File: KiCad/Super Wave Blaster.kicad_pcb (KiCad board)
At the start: 2 copper layers, 40 x 21.2 mm, 21 parts, among them J1 EIAJ_Input, J2 PCM5102_I2S, J3 PCM5102_Audio, J4 Power Input, J5 Audio_Jack, J6 Power Input, J7 Audio Out, U1 TLV73333PDBV, U2 CD74HCT14PWR, U3 SN74HC595PWR, U4 SN74LVC8T245PWR

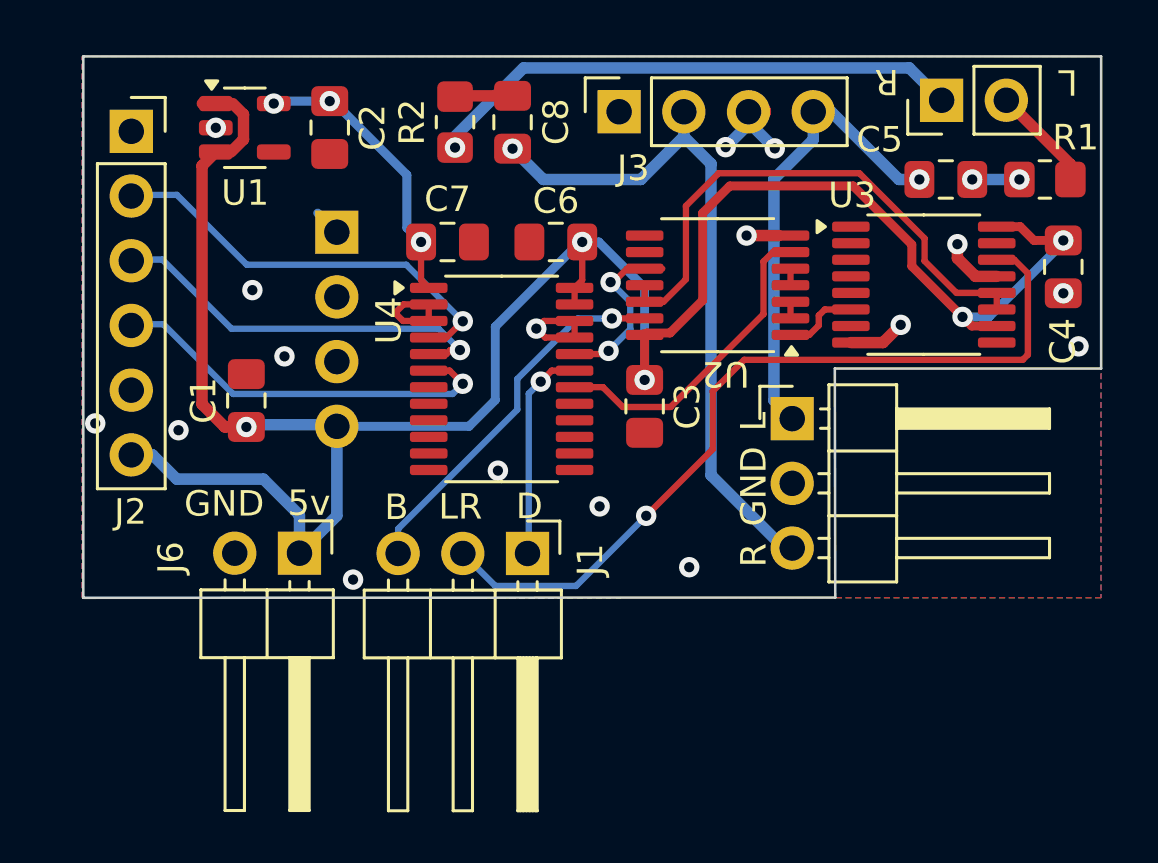
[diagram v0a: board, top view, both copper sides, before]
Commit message: V1.5
Refactored for underside mounting only and optional expansion for S/PDIF output. Full PCM5102A integration. Optimized audio quality.
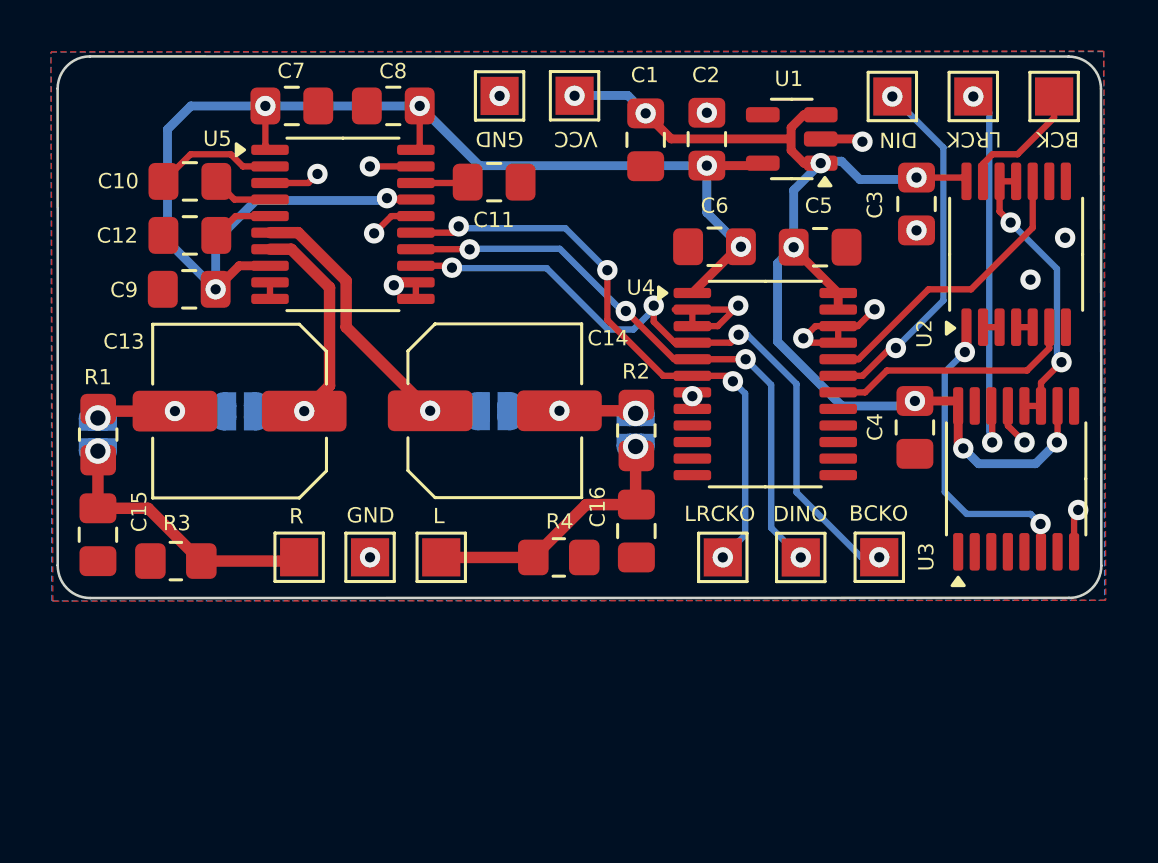
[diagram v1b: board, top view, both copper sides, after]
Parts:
- removed J1: EIAJ_Input, Connector_PinHeader_2.54mm:PinHeader_1x03_P2.54mm_Horizontal
- removed J2: PCM5102_I2S, Connector_PinSocket_2.54mm:PinSocket_1x06_P2.54mm_Vertical
- removed J3: PCM5102_Audio, Connector_PinSocket_2.54mm:PinSocket_1x04_P2.54mm_Vertical
- removed J4: Power Input, Connector_PinHeader_2.54mm:PinHeader_1x04_P2.54mm_Vertical
- removed J5: Audio_Jack, Connector_PinHeader_2.54mm:PinHeader_1x03_P2.54mm_Horizontal
- removed J6: Power Input, Connector_PinHeader_2.54mm:PinHeader_1x02_P2.54mm_Horizontal
- removed J7: Audio Out, Connector_PinHeader_2.54mm:PinHeader_1x02_P2.54mm_Vertical
- added C10: 2.2uf, Capacitor_SMD:C_0805_2012Metric_Pad1.18x1.45mm_HandSolder, F.Cu at (118.5, 68.7)
- added C11: 0.1uf, Capacitor_SMD:C_0805_2012Metric_Pad1.18x1.45mm_HandSolder, F.Cu at (130.4, 68.7)
- added C12: 2.2uf, Capacitor_SMD:C_0805_2012Metric_Pad1.18x1.45mm_HandSolder, F.Cu at (118.5, 70.8)
- added C13: 1uf, Capacitor_SMD:C_Elec_6.3x5.8, F.Cu at (120.4, 77.7)
- added C14: 1uf, Capacitor_SMD:C_Elec_6.3x5.8, F.Cu at (130.5, 77.7)
- added C15: 43pf, Capacitor_SMD:C_0805_2012Metric_Pad1.18x1.45mm_HandSolder, F.Cu at (114.9, 82.5)
- added C16: 43pf, Capacitor_SMD:C_0805_2012Metric_Pad1.18x1.45mm_HandSolder, F.Cu at (136.0, 82.4)
- added C9: 0.1uf, Capacitor_SMD:C_0805_2012Metric_Pad1.18x1.45mm_HandSolder, F.Cu at (118.5, 72.9)
- added JP1: ~, Jumper:SolderJumper-2_P1.3mm_Open_RoundedPad1.0x1.5mm, B.Cu at (114.9, 78.6)
- added JP2: ~, Jumper:SolderJumper-2_P1.3mm_Open_RoundedPad1.0x1.5mm, B.Cu at (136.0, 78.4)
- added JP3: ~, Jumper:SolderJumper-2_P1.3mm_Open_RoundedPad1.0x1.5mm, B.Cu at (120.5, 77.7)
- added JP4: ~, Jumper:SolderJumper-2_P1.3mm_Open_RoundedPad1.0x1.5mm, B.Cu at (130.4, 77.7)
- added R3: 100k, Resistor_SMD:R_0805_2012Metric_Pad1.20x1.40mm_HandSolder, F.Cu at (117.9, 83.6)
- added R4: 100k, Resistor_SMD:R_0805_2012Metric_Pad1.20x1.40mm_HandSolder, F.Cu at (133.0, 83.4)
- added TP1: VCC, TestPoint:TestPoint_Pad_1.5x1.5mm, F.Cu at (133.6, 65.3)
- added TP10: BCLKO, TestPoint:TestPoint_Pad_1.5x1.5mm, F.Cu at (145.5, 83.4)
- added TP11: GND, TestPoint:TestPoint_Pad_1.5x1.5mm, F.Cu at (125.6, 83.4)
- added TP2: GND, TestPoint:TestPoint_Pad_1.5x1.5mm, F.Cu at (130.6, 65.3)
- added TP3: A-Left, TestPoint:TestPoint_Pad_1.5x1.5mm, F.Cu at (128.3, 83.4)
- added TP4: A-Left, TestPoint:TestPoint_Pad_1.5x1.5mm, F.Cu at (122.8, 83.4)
- added TP5: DIN, TestPoint:TestPoint_Pad_1.5x1.5mm, F.Cu at (146.1, 65.3)
- added TP6: LRCLK, TestPoint:TestPoint_Pad_1.5x1.5mm, F.Cu at (149.2, 65.3)
- added TP7: BCLK, TestPoint:TestPoint_Pad_1.5x1.5mm, F.Cu at (152.4, 65.3)
- added TP8: DINO, TestPoint:TestPoint_Pad_1.5x1.5mm, F.Cu at (142.5, 83.4)
- added TP9: LRCLKO, TestPoint:TestPoint_Pad_1.5x1.5mm, F.Cu at (139.4, 83.4)
- added U5: PCM5102A, Package_SO:TSSOP-20_4.4x6.5mm_P0.65mm, F.Cu at (124.5, 70.3)
- C5, C8: value 1uf -> 0.1uf
- moved R1 38.5 mm to (114.9, 78.6), turned to 90 degrees
- moved U1 21.5 mm to (142.1, 67.0), turned to 180 degrees
- moved C1 18.7 mm to (136.4, 67.0), turned to -90 degrees
- moved C2 14.8 mm to (138.8, 67.0), turned to 90 degrees
- moved R2 14.0 mm to (136.0, 78.4), turned to 90 degrees
- moved C3 13.3 mm to (147.0, 69.5)
- moved U2 11.8 mm to (150.9, 71.5), turned to 90 degrees
- moved U4 10.4 mm to (141.1, 76.6)
- moved C4 8.58 mm to (146.9, 78.3)
- moved U3 8.44 mm to (150.9, 80.3), turned to 90 degrees
- moved C7 8.12 mm to (122.5, 65.7)
- moved C6 6.23 mm to (139.1, 71.2)
- moved C5 5.61 mm to (143.2, 71.2)
- moved C8 4.73 mm to (126.5, 65.7), turned to 180 degrees
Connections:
- C5 pad 1: AUDIO_L -> VCC
- C5 pad 2: Net-(C5-Pad2) -> GND
- C6 pad 1: VCC -> VDD
- C8 pad 1: AUDIO_R -> VDD
- C8 pad 2: Net-(C8-Pad2) -> GND
- R1 pad 1: Net-(C5-Pad2) -> AUDIO_R
- R2 pad 1: Net-(C8-Pad2) -> AUDIO_L
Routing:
- net VDD: track 11.3 -> 54.7 mm, vias 3 -> 6
- net VCC: track 87.9 -> 45.4 mm, vias 5 -> 8
- net LRCK_EIAJ: track 32.4 -> 14.9 mm, vias 1 -> 2
- net Net-(JP2-A): track 21.2 -> 4.97 mm, vias 1 -> 2
- net AUDIO_R: track 27.0 -> 11.2 mm
- net Net-(JP4-A): track 0.00 -> 12.0 mm, vias 0 -> 1
- net BCK_VDD: track 16.0 -> 27.1 mm, vias 1 -> 4
- net Net-(JP3-A): track 0.00 -> 10.7 mm, vias 0 -> 1
- net BCK_INV: track 21.4 -> 11.5 mm, vias 0 -> 2
- net BCK_EIAJ: track 14.8 -> 5.06 mm, vias 1 -> 0
- net LRCK_VDD: track 15.2 -> 24.5 mm, vias 1 -> 4
- net Net-(U2-1A): track 3.01 -> 12.2 mm, vias 0 -> 2
- net DIN_VDD: track 15.0 -> 23.4 mm, vias 1 -> 4
- net AUDIO_L: track 18.2 -> 10.8 mm
- net DIN_EIAJ: track 8.47 -> 14.2 mm, vias 1 -> 2
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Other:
- board size 40 x 21.2 mm -> 41 x 21.3 mm
- board text added: "(JP1 JP2 = X R3 R4) (JP3 JP4 = X C13 C14)"
- board text added: "BCKO"
- board text added: "DINO"
- board text added: "LRCKO"
- board text added: "Super Wave Blaster V1.5 github.com/RetroLoom/Super-Wave-Blaster"
- board text added: "VCC"
- board text removed: "+"
- board text removed: "-"
- board text removed: "5v"
- board text removed: "B"
- board text removed: "D"
- board text removed: "LR"
- board text removed: "Super Wave Blaster"
- board text removed: "V1.4"

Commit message: V1.6
Refactor analog circuit with 0.1uf coupling and 100k pull down.
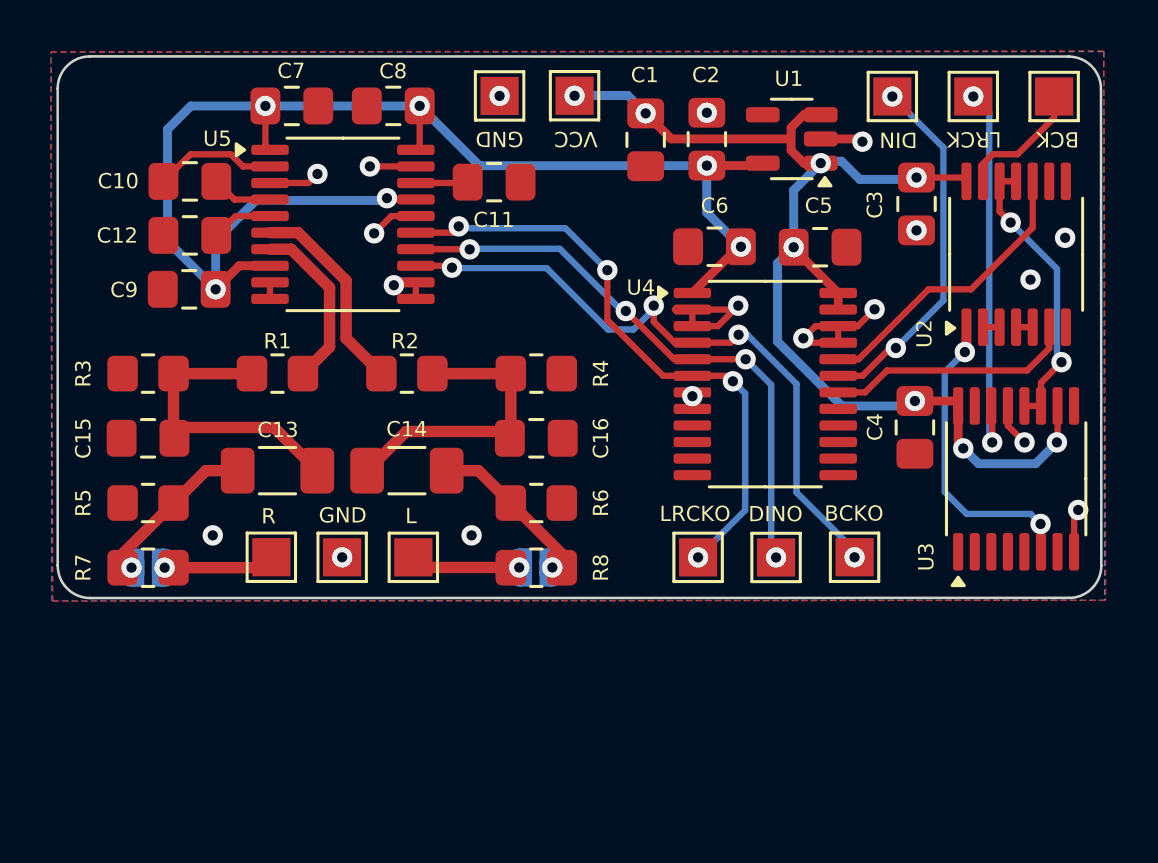
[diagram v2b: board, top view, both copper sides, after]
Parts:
- removed JP3, JP4: ~, Jumper:SolderJumper-2_P1.3mm_Open_RoundedPad1.0x1.5mm
- added R5: 100k, Resistor_SMD:R_0805_2012Metric_Pad1.20x1.40mm_HandSolder, F.Cu at (116.8, 81.3)
- added R6: 100k, Resistor_SMD:R_0805_2012Metric_Pad1.20x1.40mm_HandSolder, F.Cu at (132.1, 81.3)
- added R7: 24k, Resistor_SMD:R_0805_2012Metric_Pad1.20x1.40mm_HandSolder, F.Cu at (116.8, 83.8)
- added R8: 24k, Resistor_SMD:R_0805_2012Metric_Pad1.20x1.40mm_HandSolder, F.Cu at (132.1, 83.8)
- C13, C14: value 1uf -> 0.1uf; footprint Capacitor_SMD:C_Elec_6.3x5.8 -> Capacitor_SMD:C_1206_3216Metric_Pad1.33x1.80mm_HandSolder
- C15, C16: value 43pf -> 2.2nf
- R1, R2: value 24k -> 470
- R3, R4: value 100k -> 470
- moved R2 9.28 mm to (127.0, 76.2), turned to 180 degrees
- moved R3 7.44 mm to (116.8, 76.2)
- moved R1 7.43 mm to (121.9, 76.2), turned to 0 degrees
- moved R4 7.27 mm to (132.1, 76.2)
- moved JP2 6.67 mm to (132.1, 83.8), turned to 180 degrees
- moved JP1 5.59 mm to (116.8, 83.8), turned to 0 degrees
- moved C16 5.35 mm to (132.1, 78.7), turned to 0 degrees
- moved C15 4.27 mm to (116.8, 78.7), turned to 0 degrees
- moved C14 4.18 mm to (127.0, 80.0), turned to 180 degrees
- moved C13 2.77 mm to (121.9, 80.0), turned to 0 degrees
- moved TP11 1.09 mm to (124.5, 83.4)
- moved TP4 1.09 mm to (121.7, 83.4)
- moved TP3 1.09 mm to (127.3, 83.4)
- moved TP10 0.97 mm to (144.6, 83.4)
- moved TP8 0.97 mm to (141.5, 83.4)
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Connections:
- C13 pad 1: Net-(JP3-A) -> Net-(JP1-A)
- C13 pad 2: Net-(JP1-A) -> Net-(C13-Pad2)
- C14 pad 1: Net-(JP4-A) -> Net-(JP2-A)
- C14 pad 2: Net-(JP2-A) -> Net-(C14-Pad2)
- C15 pad 2: AUDIO_R -> Net-(C13-Pad2)
- C16 pad 1: AUDIO_L -> Net-(C14-Pad2)
- R1 pad 1: AUDIO_R -> Net-(C13-Pad2)
- R1 pad 2: Net-(JP1-A) -> Net-(U5-OUTR)
- R2 pad 1: AUDIO_L -> Net-(C14-Pad2)
- R2 pad 2: Net-(JP2-A) -> Net-(U5-OUTL)
- R3 pad 1: AUDIO_R -> Net-(C13-Pad2)
- R4 pad 2: AUDIO_L -> Net-(C14-Pad2)
- U5 pad 6: Net-(JP4-A) -> Net-(U5-OUTL)
- U5 pad 7: Net-(JP3-A) -> Net-(U5-OUTR)
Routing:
- net Net-(C13-Pad2): track 0.00 -> 12.1 mm
- net Net-(JP4-A): track 12.0 -> 0.00 mm, vias 1 -> 0
- net Net-(C14-Pad2): track 0.00 -> 12.0 mm
- net Net-(JP3-A): track 10.7 -> 0.00 mm, vias 1 -> 0
- net Net-(U5-OUTL): track 0.00 -> 7.99 mm
- net AUDIO_R: track 11.2 -> 4.36 mm
- net Net-(U5-OUTR): track 0.00 -> 6.77 mm
- net AUDIO_L: track 10.8 -> 4.32 mm
- net Net-(JP2-A): track 4.97 -> 6.41 mm, vias 2 -> 1
- net Net-(JP1-A): track 5.00 -> 6.41 mm, vias 2 -> 1
- net BCK_VDD: track 27.1 -> 26.3 mm
- net GND: vias 17 -> 19
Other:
- board text added: "(JP1 JP2 = X R7 R8)"
- board text added: "Super Wave Blaster V1.6 github.com/RetroLoom/Super-Wave-Blaster"
- board text removed: "(JP1 JP2 = X R3 R4) (JP3 JP4 = X C13 C14)"
- board text removed: "Super Wave Blaster V1.5 github.com/RetroLoom/Super-Wave-Blaster"

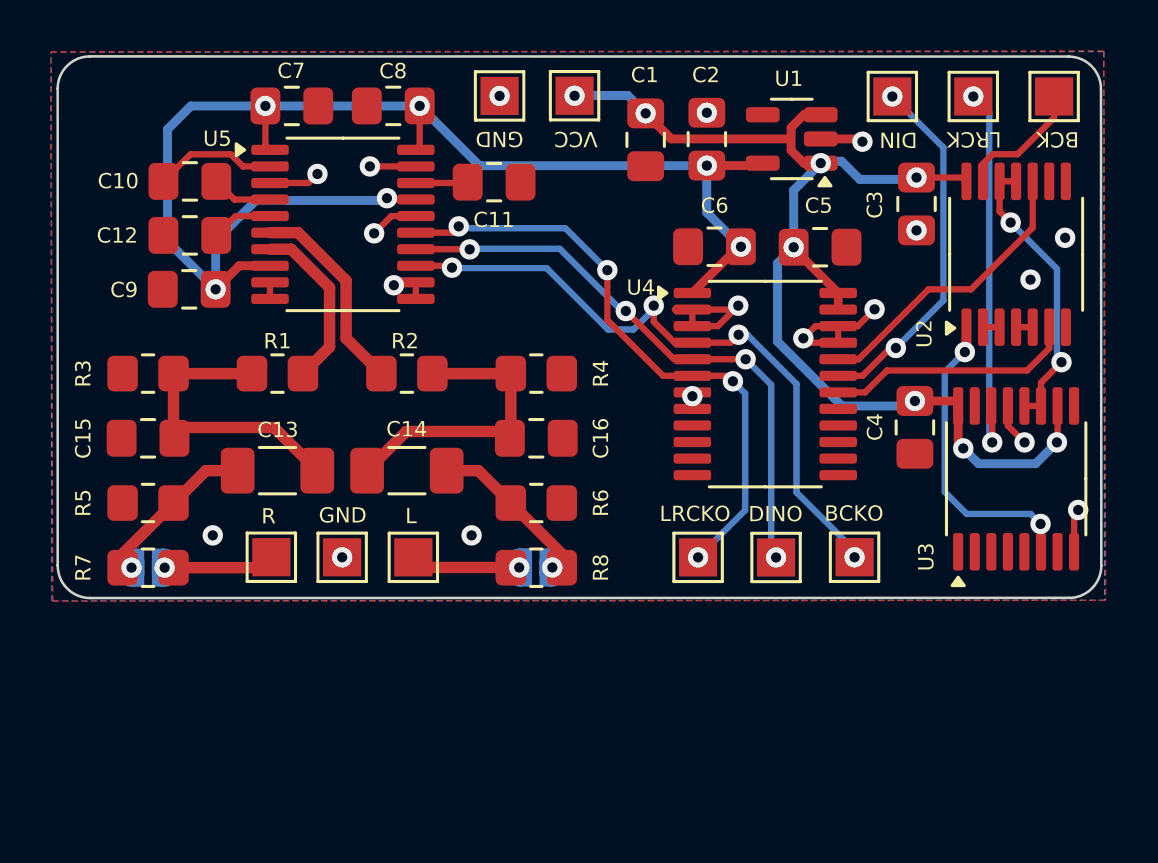
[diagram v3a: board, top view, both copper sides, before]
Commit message: v1.7 - Fix issue with high pass pole, add MDF measurements, update layout for changes with X7R coupling caps
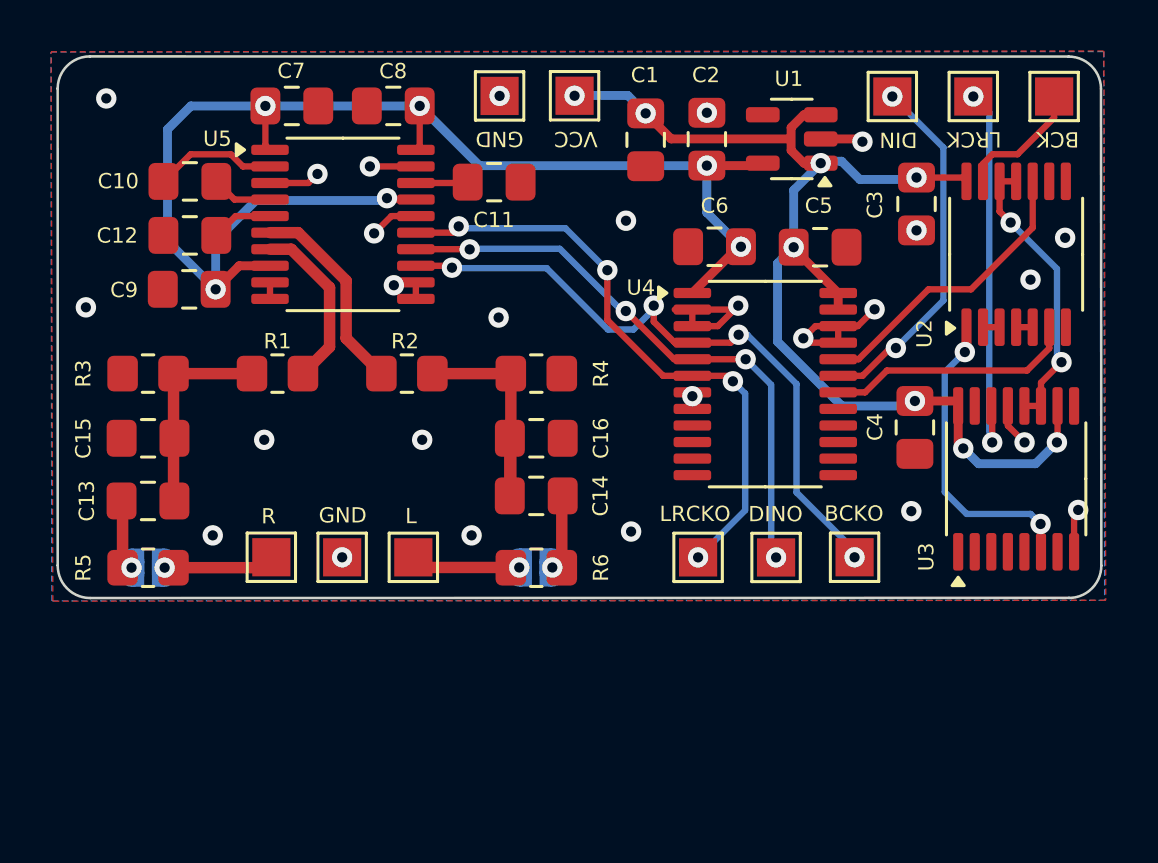
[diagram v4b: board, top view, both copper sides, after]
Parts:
- removed the R5 at (116.8, 81.3)
- removed the R6 at (132.1, 81.3)
- C13, C14: value 0.1uf -> 1uF; footprint Capacitor_SMD:C_1206_3216Metric_Pad1.33x1.80mm_HandSolder -> Capacitor_SMD:C_0805_2012Metric_Pad1.18x1.45mm_HandSolder
- R3, R4: value 470 -> 10k
- moved C13 5.22 mm to (116.8, 81.2)
- moved C14 5.17 mm to (132.1, 81.0)
- renumbered R7 to R5, R8 to R6
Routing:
- net Net-(JP2-A): track 6.41 -> 2.29 mm
- net Net-(C13-Pad2): track 12.1 -> 8.09 mm
- net Net-(JP1-A): track 6.41 -> 2.64 mm
- net Net-(C14-Pad2): track 12.0 -> 10.5 mm
- net GND: vias 19 -> 27
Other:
- board text added: "Super Wave Blaster V1.7 github.com/RetroLoom/Super-Wave-Blaster"
- board text removed: "Super Wave Blaster V1.6 github.com/RetroLoom/Super-Wave-Blaster"
